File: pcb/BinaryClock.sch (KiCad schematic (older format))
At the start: 20 parts, among them CON1 AVR-ISP-6, CON2 BARREL_JACK, IC1 ATMEGA328P-A, U1 MC33269, U2 DS3231, U3 clock_header, U4 clock_header, U5 clock_header, Y1 16MHz

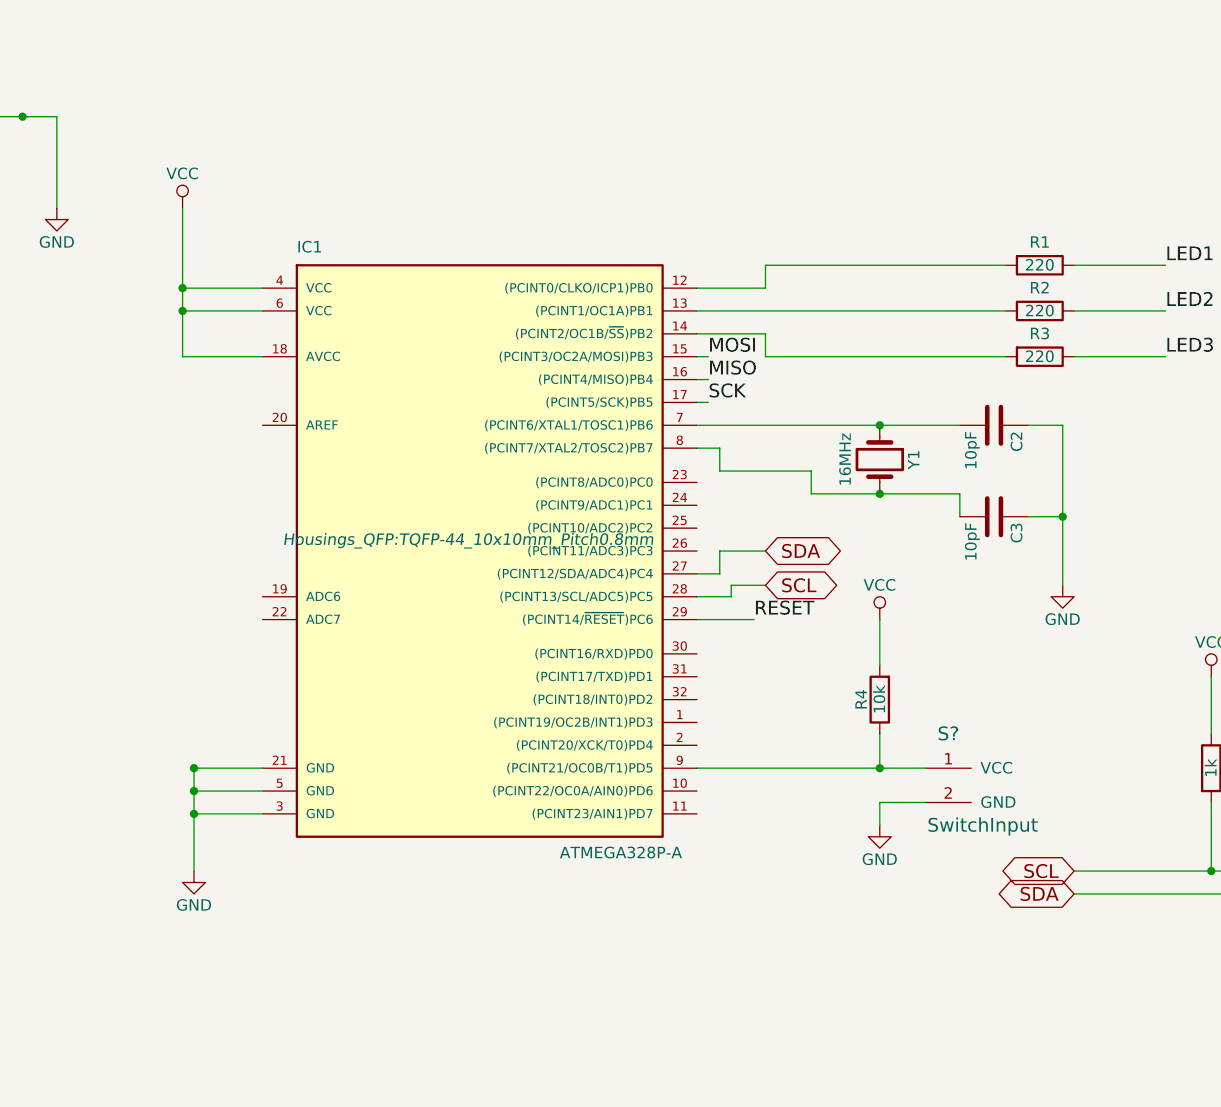
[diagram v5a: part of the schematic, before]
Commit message: Changed atmega328 schematic part to be used from a different kicad library
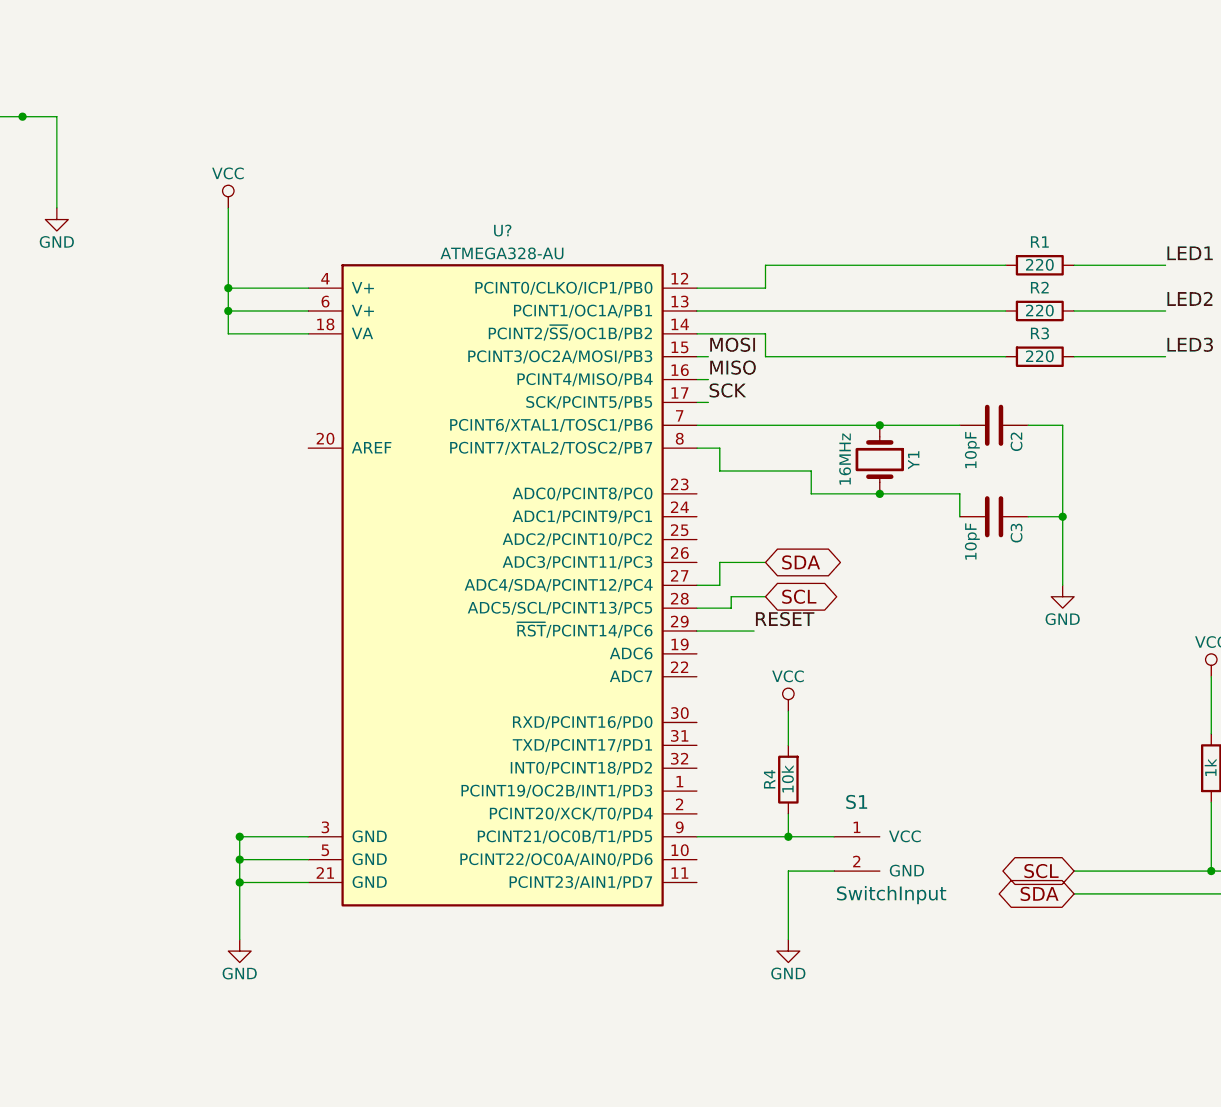
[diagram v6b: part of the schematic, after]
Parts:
- removed IC1: ATMEGA328P-A, Housings_QFP:TQFP-44_10x10mm_Pitch0.8mm, symbol ATMEGA328P-A
- added U?: ATMEGA328-AU, IPC7351-Nominal:QFP80P900X900X120-32, symbol ATMEGA328-AU
- gave numbers to parts that had none: 1
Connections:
- net GND: now also U?.21 (GND), U?.3 (GND), U?.5 (GND)
- net MISO: now also U?.16 (PCINT4/MISO/PB4)
- net MOSI: now also U?.15 (PCINT3/OC2A/MOSI/PB3)
- net RESET: now also U?.29 (~RST~/PCINT14/PC6)
- net SCK: now also U?.17 (SCK/PCINT5/PB5)
- net SCL: now also U?.28 (ADC5/SCL/PCINT13/PC5)
- net SDA: now also U?.27 (ADC4/SDA/PCINT12/PC4)
- net VCC: now also U?.18 (VA), U?.4 (V+), U?.6 (V+)
- net at C2.2, Y1.1: now also U?.7 (PCINT6/XTAL1/TOSC1/PB6)
- net at C3.2, Y1.2: now also U?.8 (PCINT7/XTAL2/TOSC2/PB7)
- net at R1.2: now also U?.12 (PCINT0/CLKO/ICP1/PB0)
- net at R2.2: now also U?.13 (PCINT1/OC1A/PB1)
- net at R3.2: now also U?.14 (PCINT2/~SS~/OC1B/PB2)
- net at R4.1, S1.1 (VCC): now also U?.9 (PCINT21/OC0B/T1/PD5)
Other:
- moved on the sheet: R4, S1
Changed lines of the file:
@@
 LIBS:maxim
 LIBS:binaryclock
+LIBS:Atmel
 LIBS:BinaryClock-cache
 EELAYER 25 0
@@
 L VCC #PWR02
 U 1 1 5888112B
-P 4050 1900
-F 0 "#PWR02" H 4050 1750 50  0001 C CNN
-F 1 "VCC" H 4050 2050 50  0000 C CNN
-F 2 "" H 4050 1900 50  0000 C CNN
-F 3 "" H 4050 1900 50  0000 C CNN
-	1    4050 1900
+P 4250 1900
+F 0 "#PWR02" H 4250 1750 50  0001 C CNN
+F 1 "VCC" H 4250 2050 50  0000 C CNN
+F 2 "" H 4250 1900 50  0000 C CNN
+F 3 "" H 4250 1900 50  0000 C CNN
+	1    4250 1900
 	1    0    0    -1
 $EndComp
@@
 Text Label 8350 2550 0    60   ~ 0
 LED3
-Text GLabel 6600 3550 2    60   BiDi ~ 0
+Text GLabel 6600 3600 2    60   BiDi ~ 0
 SCL
-Text GLabel 6600 3400 2    60   BiDi ~ 0
+Text GLabel 6600 3450 2    60   BiDi ~ 0
 SDA
 Text GLabel 7950 4900 0    60   BiDi ~ 0
@@
 L GND #PWR08
 U 1 1 58885855
-P 4100 4800
-F 0 "#PWR08" H 4100 4550 50  0001 C CNN
-F 1 "GND" H 4100 4650 50  0000 C CNN
-F 2 "" H 4100 4800 50  0000 C CNN
-F 3 "" H 4100 4800 50  0000 C CNN
-	1    4100 4800
-	1    0    0    -1
-$EndComp
-$Comp
-L ATMEGA328P-A IC1
-U 1 1 589159C8
-P 5300 3350
-F 0 "IC1" H 4550 4600 50  0000 L BNN
-F 1 "ATMEGA328P-A" H 5700 1950 50  0000 L BNN
-F 2 "Housings_QFP:TQFP-44_10x10mm_Pitch0.8mm" H 5300 3350 50  0000 C CIN
-F 3 "" H 5300 3350 50  0000 C CNN
-	1    5300 3350
+P 4300 5100
+F 0 "#PWR08" H 4300 4850 50  0001 C CNN
+F 1 "GND" H 4300 4950 50  0000 C CNN
+F 2 "" H 4300 5100 50  0000 C CNN
+F 3 "" H 4300 5100 50  0000 C CNN
+	1    4300 5100
 	1    0    0    -1
 $EndComp
@@
 Text Label 1750 3150 2    60   ~ 0
 MISO
-Text Label 6550 3700 0    60   ~ 0
+Text Label 6550 3750 0    60   ~ 0
 RESET
 Text Label 2800 3250 0    60   ~ 0
@@
 L R R4
 U 1 1 5929A12D
-P 7100 4050
-F 0 "R4" V 7180 4050 50  0000 C CNN
-F 1 "10k" V 7100 4050 50  0000 C CNN
-F 2 "" V 7030 4050 50  0000 C CNN
-F 3 "" H 7100 4050 50  0000 C CNN
-	1    7100 4050
+P 6700 4400
+F 0 "R4" V 6780 4400 50  0000 C CNN
+F 1 "10k" V 6700 4400 50  0000 C CNN
+F 2 "" V 6630 4400 50  0000 C CNN
+F 3 "" H 6700 4400 50  0000 C CNN
+	1    6700 4400
 	-1   0    0    1
+$EndComp
+$Comp
+L GND #PWR?
+U 1 1 5929BBA2
+P 6700 5100
+F 0 "#PWR?" H 6700 4850 50  0001 C CNN
+F 1 "GND" H 6700 4950 50  0000 C CNN
+F 2 "" H 6700 5100 50  0000 C CNN
+F 3 "" H 6700 5100 50  0000 C CNN
+	1    6700 5100
+	1    0    0    -1
+$EndComp
+$Comp
+L VCC #PWR?
+U 1 1 5929BE36
+P 6700 4100
+F 0 "#PWR?" H 6700 3950 50  0001 C CNN
+F 1 "VCC" H 6700 4250 50  0000 C CNN
+F 2 "" H 6700 4100 50  0000 C CNN
+F 3 "" H 6700 4100 50  0000 C CNN
+	1    6700 4100
+	1    0    0    -1
+$EndComp
+$Comp
+L SwitchInput S1
+U 1 1 5929C320
+P 6900 4650
+F 0 "S1" H 7000 4800 60  0000 C CNN
+F 1 "SwitchInput" H 7150 4400 60  0000 C CNN
+F 2 "" H 6900 4650 60  0001 C CNN
+F 3 "" H 6900 4650 60  0001 C CNN
+	1    6900 4650
+	1    0    0    -1
+$EndComp
+$Comp
+L ATMEGA328-AU U?
+U 1 1 5929C7F4
+P 5450 3550
+F 0 "U?" H 5450 5100 50  0000 C CNN
+F 1 "ATMEGA328-AU" H 5450 5000 50  0000 C CNN
+F 2 "IPC7351-Nominal:QFP80P900X900X120-32" H 5450 2050 50  0001 C CNN
+F 3 "http://www.atmel.com/images/Atmel-8271-8-bit-AVR-Microcontroller-ATmega48A-48PA-88A-88PA-168A-168PA-328-328P_datasheet_Complete.pdf" H 5450 1950 50  0001 C CNN
+F 4 "ATMEGA328-AU" H 5450 1650 50  0001 C CNN "MPN"
+F 5 "Microchip" H 5450 1750 50  0001 C CNN "Manuf"
+F 6 "Microchip ATMEGA328-AU" H 5450 1850 50  0001 C CNN "BOM"
+	1    5450 3550
+	1    0    0    -1
 $EndComp
 Wire Wire Line
@@
 	8850 4500 8850 4900
 Wire Wire Line
-	4050 1900 4050 2550
-Wire Wire Line
-	4050 2350 4400 2350
-Wire Wire Line
-	4400 2250 4050 2250
-Connection ~ 4050 2250
-Wire Wire Line
-	4400 4350 4100 4350
-Wire Wire Line
-	4400 4450 4100 4450
-Connection ~ 4100 4450
-Wire Wire Line
-	4100 4550 4400 4550
-Connection ~ 4100 4550
-Connection ~ 4100 4350
+	4250 1900 4250 2450
+Wire Wire Line
+	4250 2350 4600 2350
+Wire Wire Line
+	4600 2250 4250 2250
+Connection ~ 4250 2250
+Wire Wire Line
+	4600 4650 4300 4650
+Wire Wire Line
+	4600 4750 4300 4750
+Connection ~ 4300 4750
+Wire Wire Line
+	4300 4850 4600 4850
+Connection ~ 4300 4850
+Connection ~ 4300 4650
 Wire Wire Line
 	6400 3050 6400 2950
@@
 	6300 2750 6350 2750
 Wire Wire Line
-	6300 3500 6400 3500
-Wire Wire Line
-	6400 3500 6400 3400
-Wire Wire Line
-	6400 3400 6600 3400
-Wire Wire Line
-	6300 3600 6450 3600
-Wire Wire Line
-	6450 3600 6450 3550
-Wire Wire Line
-	6450 3550 6600 3550
+	6300 3550 6400 3550
+Wire Wire Line
+	6400 3550 6400 3450
+Wire Wire Line
+	6400 3450 6600 3450
+Wire Wire Line
+	6300 3650 6450 3650
+Wire Wire Line
+	6450 3650 6450 3600
+Wire Wire Line
+	6450 3600 6600 3600
 Wire Wire Line
 	1750 3150 2150 3150
@@
 	3100 1500 3500 1500
 Wire Wire Line
-	4100 4350 4100 4800
+	4300 4650 4300 5100
 Wire Wire Line
 	2700 2150 3100 2150
@@
 Connection ~ 3350 1500
 Wire Wire Line
-	6550 3700 6300 3700
+	6550 3750 6300 3750
 Wire Wire Line
 	2750 2750 1300 2750
@@
 	1300 3100 1300 3350
 Connection ~ 1300 3350
-Wire Wire Line
-	4050 2550 4400 2550
-Connection ~ 4050 2350
+Connection ~ 4250 2350
 Wire Wire Line
 	8550 3950 8550 4200
@@
 Wire Wire Line
 	1550 900  1550 700
-$Comp
-L GND #PWR?
-U 1 1 5929BBA2
-P 7100 4600
-F 0 "#PWR?" H 7100 4350 50  0001 C CNN
-F 1 "GND" H 7100 4450 50  0000 C CNN
-F 2 "" H 7100 4600 50  0000 C CNN
-F 3 "" H 7100 4600 50  0000 C CNN
-	1    7100 4600
-	1    0    0    -1
-$EndComp
-$Comp
-L VCC #PWR?
-U 1 1 5929BE36
-P 7100 3700
-F 0 "#PWR?" H 7100 3550 50  0001 C CNN
-F 1 "VCC" H 7100 3850 50  0000 C CNN
-F 2 "" H 7100 3700 50  0000 C CNN
-F 3 "" H 7100 3700 50  0000 C CNN
-	1    7100 3700
-	1    0    0    -1
-$EndComp
-Wire Wire Line
-	7100 3700 7100 3900
-$Comp
-L SwitchInput S?
-U 1 1 5929C320
-P 7300 4350
-F 0 "S?" H 7400 4500 60  0000 C CNN
-F 1 "SwitchInput" H 7550 4100 60  0000 C CNN
-F 2 "" H 7300 4350 60  0001 C CNN
-F 3 "" H 7300 4350 60  0001 C CNN
-	1    7300 4350
-	1    0    0    -1
-$EndComp
-Wire Wire Line
-	6300 4350 7300 4350
-Wire Wire Line
-	7100 4200 7100 4350
-Connection ~ 7100 4350
-Wire Wire Line
-	7300 4500 7100 4500
-Wire Wire Line
-	7100 4500 7100 4600
+Wire Wire Line
+	6300 4650 6900 4650
+Wire Wire Line
+	6700 4550 6700 4650
+Connection ~ 6700 4650
+Wire Wire Line
+	6700 4100 6700 4250
+Wire Wire Line
+	6900 4800 6700 4800
+Wire Wire Line
+	6700 4800 6700 5100
+Wire Wire Line
+	4250 2450 4600 2450
 $EndSCHEMATC

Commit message: Removed old bogus atmega328 footprint, replaced with correct TQFP32
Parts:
- gave numbers to parts that had none: 1
- renumbered R4 to R7
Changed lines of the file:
@@
 VIN
 $Comp
-L R R4
+L R R7
 U 1 1 5929A12D
 P 6700 4400
-F 0 "R4" V 6780 4400 50  0000 C CNN
+F 0 "R7" V 6780 4400 50  0000 C CNN
 F 1 "10k" V 6700 4400 50  0000 C CNN
 F 2 "" V 6630 4400 50  0000 C CNN
@@
 $EndComp
 $Comp
-L GND #PWR?
+L GND #PWR015
 U 1 1 5929BBA2
 P 6700 5100
-F 0 "#PWR?" H 6700 4850 50  0001 C CNN
+F 0 "#PWR015" H 6700 4850 50  0001 C CNN
 F 1 "GND" H 6700 4950 50  0000 C CNN
 F 2 "" H 6700 5100 50  0000 C CNN
@@
 $EndComp
 $Comp
-L VCC #PWR?
+L VCC #PWR016
 U 1 1 5929BE36
 P 6700 4100
-F 0 "#PWR?" H 6700 3950 50  0001 C CNN
+F 0 "#PWR016" H 6700 3950 50  0001 C CNN
 F 1 "VCC" H 6700 4250 50  0000 C CNN
 F 2 "" H 6700 4100 50  0000 C CNN
@@
 $EndComp
 $Comp
-L ATMEGA328-AU U?
+L ATMEGA328-AU U6
 U 1 1 5929C7F4
 P 5450 3550
-F 0 "U?" H 5450 5100 50  0000 C CNN
+F 0 "U6" H 5450 5100 50  0000 C CNN
 F 1 "ATMEGA328-AU" H 5450 5000 50  0000 C CNN
 F 2 "IPC7351-Nominal:QFP80P900X900X120-32" H 5450 2050 50  0001 C CNN

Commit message: Re-routing with new atmega footprint
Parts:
- S1: footprint (none) -> Pin_Headers:Pin_Header_Straight_1x02
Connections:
- net at R7.1, S1.1 (VCC): now also U6.32 (INT0/PCINT18/PD2); no longer U6.9 (PCINT21/OC0B/T1/PD5)
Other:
- moved on the sheet: R7, S1
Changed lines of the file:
@@
 L R R7
 U 1 1 5929A12D
-P 6700 4400
-F 0 "R7" V 6780 4400 50  0000 C CNN
-F 1 "10k" V 6700 4400 50  0000 C CNN
-F 2 "" V 6630 4400 50  0000 C CNN
-F 3 "" H 6700 4400 50  0000 C CNN
-	1    6700 4400
+P 7100 4100
+F 0 "R7" V 7180 4100 50  0000 C CNN
+F 1 "10k" V 7100 4100 50  0000 C CNN
+F 2 "" V 7030 4100 50  0000 C CNN
+F 3 "" H 7100 4100 50  0000 C CNN
+	1    7100 4100
 	-1   0    0    1
 $EndComp
@@
 L GND #PWR015
 U 1 1 5929BBA2
-P 6700 5100
-F 0 "#PWR015" H 6700 4850 50  0001 C CNN
-F 1 "GND" H 6700 4950 50  0000 C CNN
-F 2 "" H 6700 5100 50  0000 C CNN
-F 3 "" H 6700 5100 50  0000 C CNN
-	1    6700 5100
+P 7100 4800
+F 0 "#PWR015" H 7100 4550 50  0001 C CNN
+F 1 "GND" H 7100 4650 50  0000 C CNN
+F 2 "" H 7100 4800 50  0000 C CNN
+F 3 "" H 7100 4800 50  0000 C CNN
+	1    7100 4800
 	1    0    0    -1
 $EndComp
@@
 L VCC #PWR016
 U 1 1 5929BE36
-P 6700 4100
-F 0 "#PWR016" H 6700 3950 50  0001 C CNN
-F 1 "VCC" H 6700 4250 50  0000 C CNN
-F 2 "" H 6700 4100 50  0000 C CNN
-F 3 "" H 6700 4100 50  0000 C CNN
-	1    6700 4100
+P 7100 3800
+F 0 "#PWR016" H 7100 3650 50  0001 C CNN
+F 1 "VCC" H 7100 3950 50  0000 C CNN
+F 2 "" H 7100 3800 50  0000 C CNN
+F 3 "" H 7100 3800 50  0000 C CNN
+	1    7100 3800
 	1    0    0    -1
 $EndComp
@@
 L SwitchInput S1
 U 1 1 5929C320
-P 6900 4650
-F 0 "S1" H 7000 4800 60  0000 C CNN
-F 1 "SwitchInput" H 7150 4400 60  0000 C CNN
-F 2 "" H 6900 4650 60  0001 C CNN
-F 3 "" H 6900 4650 60  0001 C CNN
-	1    6900 4650
+P 7300 4350
+F 0 "S1" H 7400 4500 60  0000 C CNN
+F 1 "SwitchInput" H 7550 4100 60  0000 C CNN
+F 2 "Pin_Headers:Pin_Header_Straight_1x02" H 7300 4350 60  0001 C CNN
+F 3 "" H 7300 4350 60  0001 C CNN
+	1    7300 4350
 	1    0    0    -1
 $EndComp
@@
 	1550 900  1550 700
 Wire Wire Line
-	6300 4650 6900 4650
-Wire Wire Line
-	6700 4550 6700 4650
-Connection ~ 6700 4650
-Wire Wire Line
-	6700 4100 6700 4250
-Wire Wire Line
-	6900 4800 6700 4800
-Wire Wire Line
-	6700 4800 6700 5100
+	7100 3800 7100 3950
+Wire Wire Line
+	7300 4500 7100 4500
+Wire Wire Line
+	7100 4500 7100 4800
 Wire Wire Line
 	4250 2450 4600 2450
+Wire Wire Line
+	6300 4350 7300 4350
+Wire Wire Line
+	7100 4250 7100 4350
+Connection ~ 7100 4350
 $EndSCHEMATC
